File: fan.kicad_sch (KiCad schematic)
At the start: 15 parts, among them J6 Conn_01x04, J7 Conn_01x04, U10 EMC2101

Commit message: lots of misc
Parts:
- C51: value 47uF -> 100uF; footprint Capacitor_SMD:C_1210_3225Metric -> Capacitor_SMD:C_1206_3216Metric; DK 1276-3376-1-ND -> 1276-1782-1-ND; PARTNO CL32A476KOJNNNE -> CL31A107MQHNNNE
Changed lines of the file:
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@@
 			)
 		)
-		(property "Value" "47uF"
+		(property "Value" "100uF"
 			(at 138.43 122.555 0)
 			(effects
@@
 			)
 		)
-		(property "Footprint" "Capacitor_SMD:C_1210_3225Metric"
+		(property "Footprint" "Capacitor_SMD:C_1206_3216Metric"
 			(at 144.78 119.38 0)
 			(effects
@@
 			)
 		)
-		(property "DK" "1276-3376-1-ND"
+		(property "DK" "1276-1782-1-ND"
 			(at 144.78 119.38 0)
 			(effects
@@
 			)
 		)
-		(property "PARTNO" "CL32A476KOJNNNE"
+		(property "PARTNO" "CL31A107MQHNNNE"
 			(at 144.78 119.38 0)
 			(effects

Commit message: layout
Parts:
- removed J7: Conn_01x04, Connector_JST:JST_SH_BM04B-SRSS-TB_1x04-1MP_P1.00mm_Vertical, symbol Connector_Generic_MountingPin:Conn_01x04_MountingPin
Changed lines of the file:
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@@
-	)
-	(junction
-		(at 179.07 114.3)
-		(diameter 0)
-		(color 0 0 0 0)
 	)
 	(junction
@@
 	)
 	(junction
-		(at 179.07 111.76)
-		(diameter 0)
-		(color 0 0 0 0)
-	)
-	(junction
 		(at 106.68 86.36)
 		(diameter 0)
@@
 	)
 	(junction
-		(at 179.07 109.22)
-		(diameter 0)
-		(color 0 0 0 0)
-	)
-	(junction
 		(at 144.78 114.3)
-		(diameter 0)
-		(color 0 0 0 0)
-	)
-	(junction
-		(at 179.07 116.84)
 		(diameter 0)
 		(color 0 0 0 0)
@@
 	(wire
 		(pts
-			(xy 179.07 111.76) (xy 187.96 111.76)
-		)
-		(stroke
-			(width 0)
-			(type default)
-		)
-	)
-	(wire
-		(pts
 			(xy 151.13 127) (xy 167.64 127)
 		)
@@
 	(wire
 		(pts
-			(xy 179.07 116.84) (xy 187.96 116.84)
-		)
-		(stroke
-			(width 0)
-			(type default)
-		)
-	)
-	(wire
-		(pts
 			(xy 179.07 66.04) (xy 191.77 66.04)
 		)
@@
 	(wire
 		(pts
-			(xy 179.07 114.3) (xy 187.96 114.3)
-		)
-		(stroke
-			(width 0)
-			(type default)
-		)
-	)
-	(wire
-		(pts
 			(xy 157.48 83.82) (xy 191.77 83.82)
 		)
@@
 		(pts
 			(xy 134.62 127) (xy 144.78 127)
-		)
-		(stroke
-			(width 0)
-			(type default)
-		)
-	)
-	(wire
-		(pts
-			(xy 179.07 109.22) (xy 187.96 109.22)
 		)
 		(stroke
@@
 					(unit 1)
 				)
-			)
-		)
-	)
-	(symbol
-		(lib_id "Connector_Generic_MountingPin:Conn_01x04_MountingPin")
-		(at 193.04 114.3 0)
-		(mirror x)
-		(unit 1)
-		(exclude_from_sim no)
-		(in_bom yes)
-		(on_board yes)
-		(dnp no)
-		(fields_autoplaced yes)
-		(property "Reference" "J7"
-			(at 195.58 112.6743 0)
-			(effects
-				(font
-					(size 1.27 1.27)
-				)
-				(justify left)
-			)
-		)
-		(property "Value" "Conn_01x04"
-			(at 193.04 104.775 0)
-			(effects
-				(font
-					(size 1.27 1.27)
-				)
-				(hide yes)
-			)
-		)
-		(property "Footprint" "Connector_JST:JST_SH_BM04B-SRSS-TB_1x04-1MP_P1.00mm_Vertical"
-			(at 193.04 114.3 0)
-			(effects
-				(font
-					(size 1.27 1.27)
-				)
-				(hide yes)
-			)
-		)
-		(property "Datasheet" "~"
-			(at 193.04 114.3 0)
-			(effects
-				(font
-					(size 1.27 1.27)
-				)
-				(hide yes)
-			)
-		)
-		(property "Description" "Generic connectable mounting pin connector, single row, 01x04, script generated (kicad-library-utils/schlib/autogen/connector/)"
-			(at 193.04 114.3 0)
-			(effects
-				(font
-					(size 1.27 1.27)
-				)
-				(hide yes)
-			)
-		)
-		(property "PARTNO" ""
-			(at 193.04 114.3 0)
-			(effects
-				(font
-					(size 1.27 1.27)
-				)
-				(hide yes)
-			)
-		)
-		(property "DK" ""
-			(at 193.04 114.3 0)
-			(effects
-				(font
-					(size 1.27 1.27)
-				)
-				(hide yes)
-			)
-		)
-		(pin "1"
-		)
-		(pin "2"
-		)
-		(pin "3"
-		)
-		(pin "4"
-		)
-		(pin "MP"
-		)
-		(instances
-			(project "bitaxeGamma"
-				(path "/e63e39d7-6ac0-4ffd-8aa3-1841a4541b55/8e8832ea-6bf1-49d2-b3a5-32a207f555d2"
-					(reference "J7")
-					(unit 1)
-				)

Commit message: DRC/layout
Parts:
- added J7: Conn_01x04, Connector_JST:JST_SH_BM04B-SRSS-TB_1x04-1MP_P1.00mm_Vertical, symbol Connector_Generic_MountingPin:Conn_01x04_MountingPin
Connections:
- net 5V: now also J7.2 (Pin_2)
- net FAN_PWM: now also J7.4 (Pin_4)
- net FAN_TACH: now also J7.3 (Pin_3)
- net GND: now also J7.1 (Pin_1)
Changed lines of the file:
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@@
+	)
+	(junction
+		(at 179.07 116.84)
+		(diameter 0)
+		(color 0 0 0 0)
 	)
 	(junction
@@
 	)
 	(junction
+		(at 179.07 111.76)
+		(diameter 0)
+		(color 0 0 0 0)
+	)
+	(junction
 		(at 82.55 76.2)
 		(diameter 0)
@@
 	)
 	(junction
+		(at 179.07 109.22)
+		(diameter 0)
+		(color 0 0 0 0)
+	)
+	(junction
+		(at 179.07 114.3)
+		(diameter 0)
+		(color 0 0 0 0)
+	)
+	(junction
 		(at 106.68 73.66)
 		(diameter 0)
@@
 	(wire
 		(pts
+			(xy 179.07 109.22) (xy 187.96 109.22)
+		)
+		(stroke
+			(width 0)
+			(type default)
+		)
+	)
+	(wire
+		(pts
 			(xy 179.07 66.04) (xy 191.77 66.04)
 		)
@@
 	(wire
 		(pts
+			(xy 179.07 114.3) (xy 187.96 114.3)
+		)
+		(stroke
+			(width 0)
+			(type default)
+		)
+	)
+	(wire
+		(pts
 			(xy 191.77 66.04) (xy 191.77 73.66)
 		)
@@
 	(wire
 		(pts
+			(xy 179.07 116.84) (xy 187.96 116.84)
+		)
+		(stroke
+			(width 0)
+			(type default)
+		)
+	)
+	(wire
+		(pts
 			(xy 179.07 66.04) (xy 179.07 68.58)
 		)
@@
 		(pts
 			(xy 151.13 123.19) (xy 151.13 127)
+		)
+		(stroke
+			(width 0)
+			(type default)
+		)
+	)
+	(wire
+		(pts
+			(xy 179.07 111.76) (xy 187.96 111.76)
 		)
 		(stroke
@@
 					(unit 1)
 				)
+			)
+		)
+	)
+	(symbol
+		(lib_id "Connector_Generic_MountingPin:Conn_01x04_MountingPin")
+		(at 193.04 114.3 0)
+		(mirror x)
+		(unit 1)
+		(exclude_from_sim no)
+		(in_bom yes)
+		(on_board yes)
+		(dnp no)
+		(fields_autoplaced yes)
+		(property "Reference" "J7"
+			(at 195.58 112.6743 0)
+			(effects
+				(font
+					(size 1.27 1.27)
+				)
+				(justify left)
+			)
+		)
+		(property "Value" "Conn_01x04"
+			(at 193.04 104.775 0)
+			(effects
+				(font
+					(size 1.27 1.27)
+				)
+				(hide yes)
+			)
+		)
+		(property "Footprint" "Connector_JST:JST_SH_BM04B-SRSS-TB_1x04-1MP_P1.00mm_Vertical"
+			(at 193.04 114.3 0)
+			(effects
+				(font
+					(size 1.27 1.27)
+				)
+				(hide yes)
+			)
+		)
+		(property "Datasheet" "~"
+			(at 193.04 114.3 0)
+			(effects
+				(font
+					(size 1.27 1.27)
+				)
+				(hide yes)
+			)
+		)
+		(property "Description" "Generic connectable mounting pin connector, single row, 01x04, script generated (kicad-library-utils/schlib/autogen/connector/)"
+			(at 193.04 114.3 0)
+			(effects
+				(font
+					(size 1.27 1.27)
+				)
+				(hide yes)
+			)
+		)
+		(property "PARTNO" ""
+			(at 193.04 114.3 0)
+			(effects
+				(font
+					(size 1.27 1.27)
+				)
+				(hide yes)
+			)
+		)
+		(property "DK" ""
+			(at 193.04 114.3 0)
+			(effects
+				(font
+					(size 1.27 1.27)
+				)
+				(hide yes)
+			)
+		)
+		(pin "1"
+		)
+		(pin "2"
+		)
+		(pin "3"
+		)
+		(pin "4"
+		)
+		(pin "MP"
+		)
+		(instances
+			(project "bitaxeGamma"
+				(path "/e63e39d7-6ac0-4ffd-8aa3-1841a4541b55/8e8832ea-6bf1-49d2-b3a5-32a207f555d2"
+					(reference "J7")
+					(unit 1)
+				)

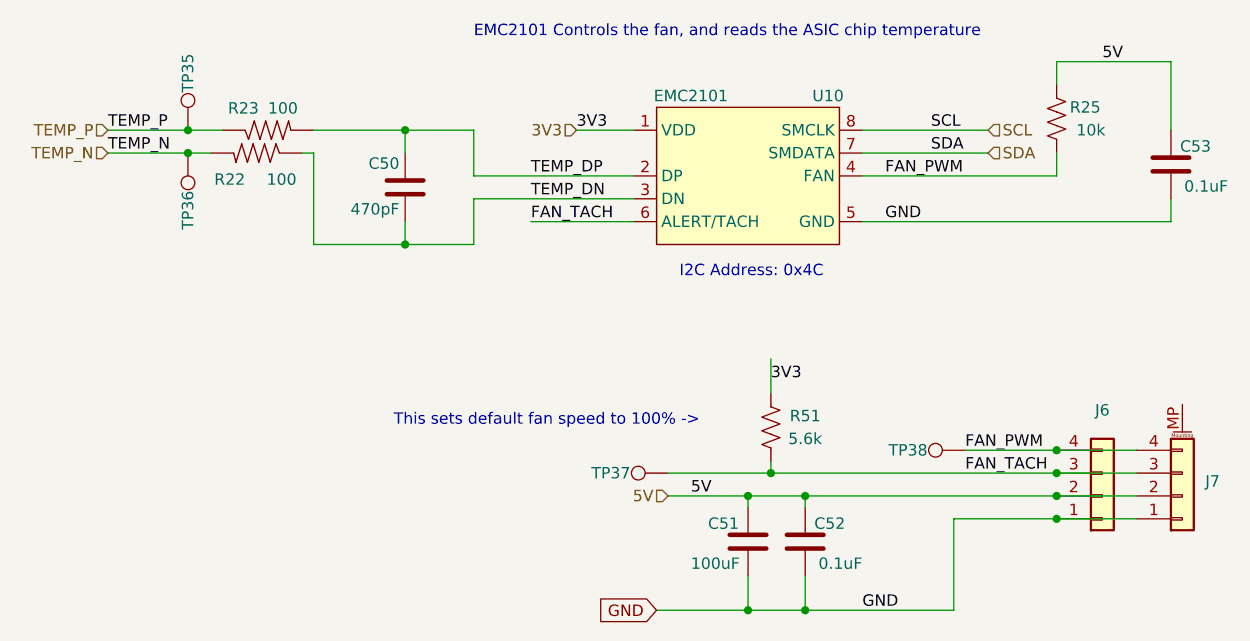
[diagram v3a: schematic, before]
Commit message: added pullup resistors for #25
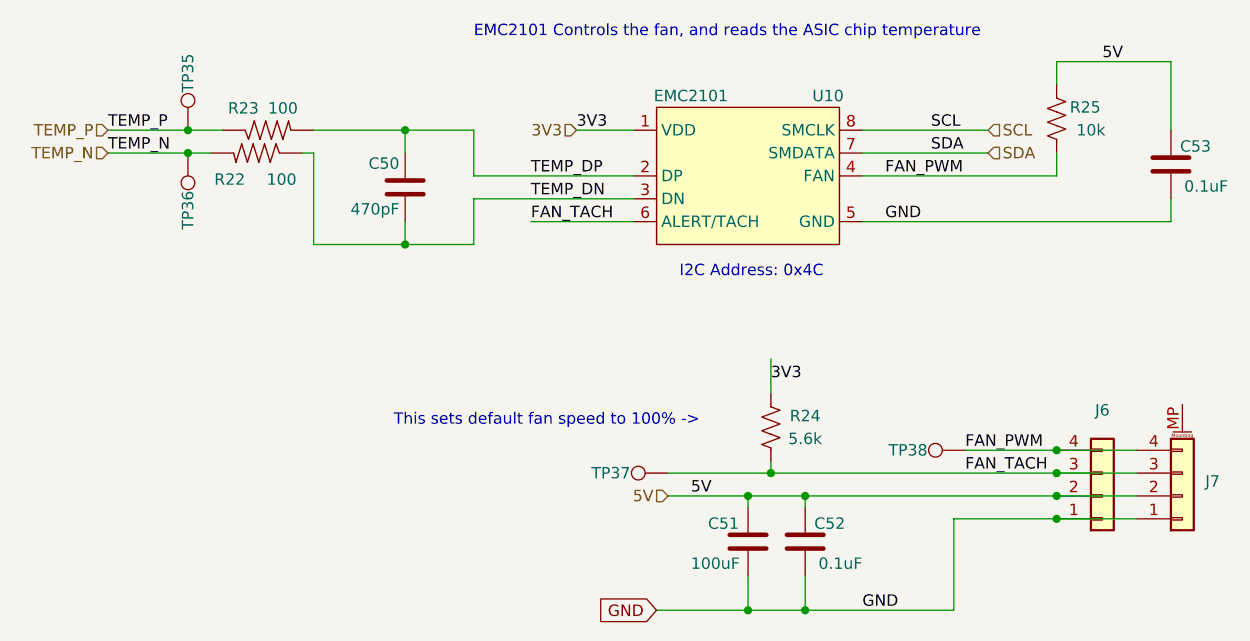
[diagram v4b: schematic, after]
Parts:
- renumbered R51 to R24

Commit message: Revert "added pullup resistors for #25"
This reverts commit 91572af801fdd590416a5d3df79444bb16faa4cf.
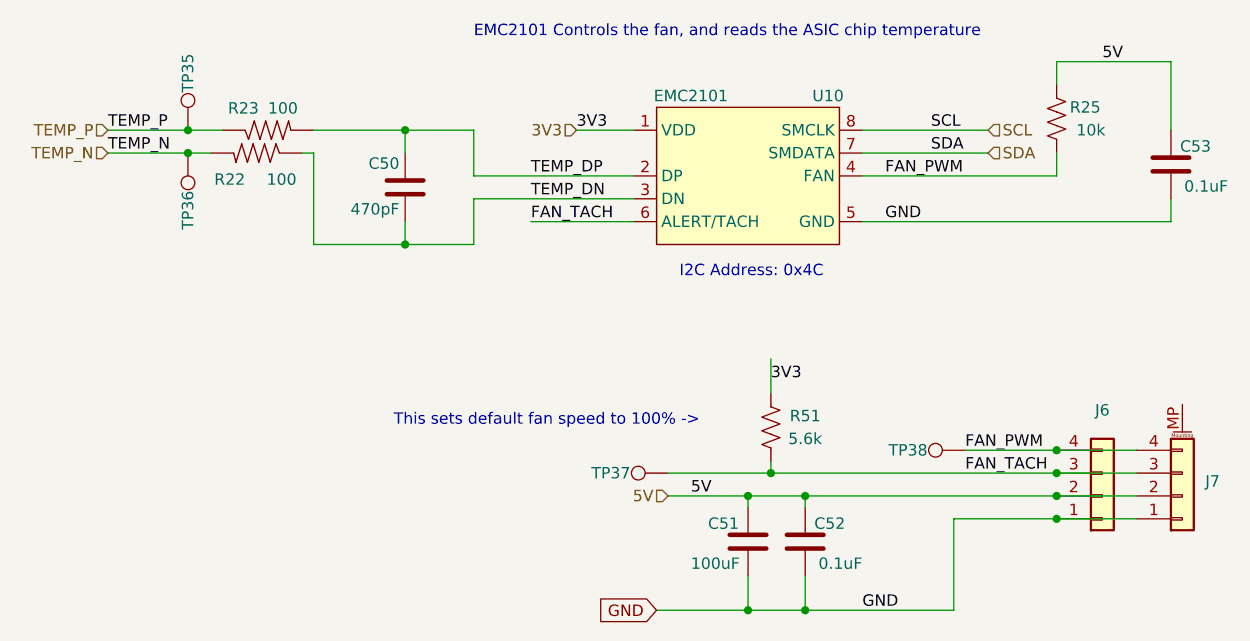
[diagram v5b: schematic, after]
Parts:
- renumbered R24 to R51
